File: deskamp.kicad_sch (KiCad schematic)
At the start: 33 parts, among them J1 Input 01, J2 Input 02, J3 Preamp Out, J4 Selector Switch, J5 LFE, J6 Mute, J7 Sleep, J8 Motor, J9 Power, K1 TQ2-12V, K2 TQ2-12V, K3 TQ2-12V, K4 TQ2-12V, Q1 PN2222A, Q2 PN2222A, Q3 PN2222A, Q4 PN2222A, U1 esp32-wemos-d1-mini, U2 L9110, U3 TSR_1-2433

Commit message: Change L9110 to Dip 8 footprint
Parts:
- U2: footprint L9110:so-8 -> Package_DIP:DIP-8_W7.62mm
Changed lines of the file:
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@@
 			)
 		)
-		(property "Footprint" "L9110:so-8"
+		(property "Footprint" "Package_DIP:DIP-8_W7.62mm"
 			(at 165.1 39.37 0)
 			(effects

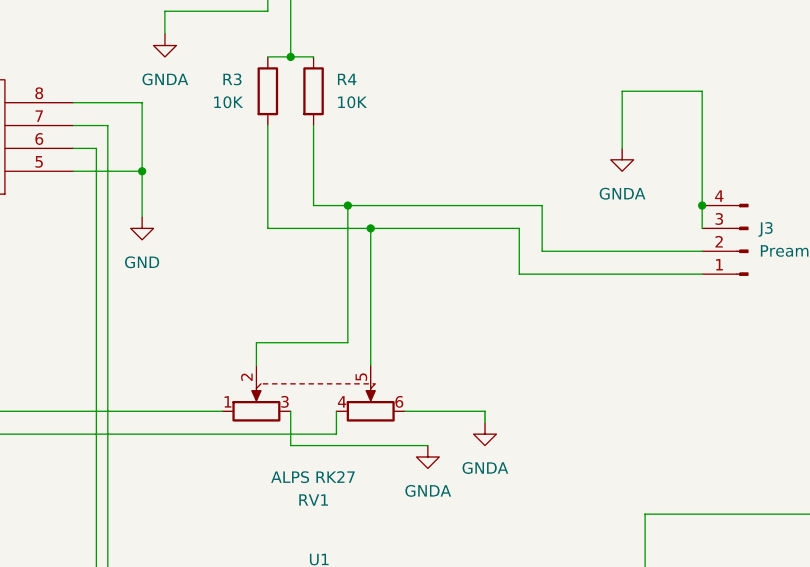
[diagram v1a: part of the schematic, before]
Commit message: Start routing signals
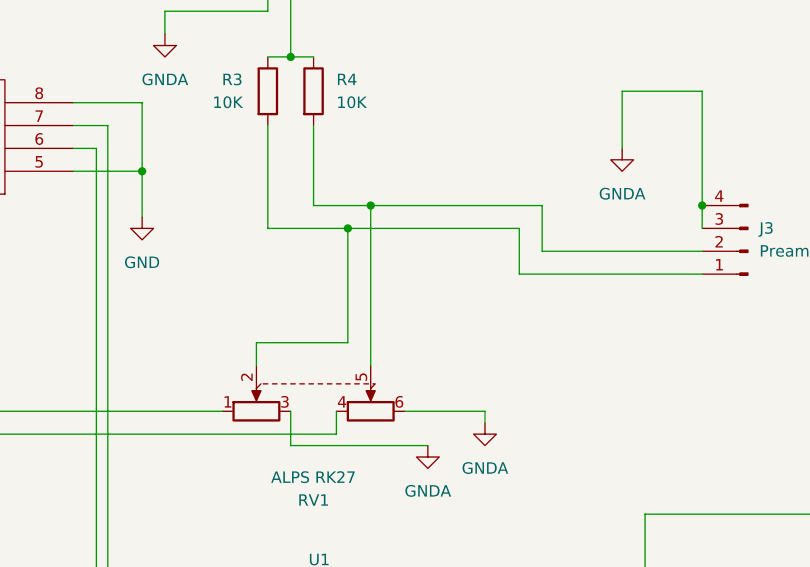
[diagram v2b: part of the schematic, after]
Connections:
- net at J3.1 (Pin_1), R3.2: now also RV1.2; no longer RV1.5
- net at J3.2 (Pin_2), R4.2: now also RV1.5; no longer RV1.2
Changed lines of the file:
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@@
 	)
 	(junction
-		(at 212.09 49.53)
+		(at 212.09 46.99)
 		(diameter 0)
 		(color 0 0 0 0)
@@
 	)
 	(junction
-		(at 209.55 46.99)
-		(diameter 0)
-		(color 0 0 0 0)
-	)
-	(junction
 		(at 151.13 38.1)
 		(diameter 0)
@@
 	)
 	(junction
+		(at 209.55 49.53)
+		(diameter 0)
+		(color 0 0 0 0)
+	)
+	(junction
 		(at 36.83 66.04)
 		(diameter 0)
@@
 	(wire
 		(pts
-			(xy 209.55 46.99) (xy 231.14 46.99)
+			(xy 205.74 46.99) (xy 212.09 46.99)
 		)
 		(stroke
@@
 	(wire
 		(pts
+			(xy 212.09 46.99) (xy 212.09 64.77)
+		)
+		(stroke
+			(width 0)
+			(type default)
+		)
+	)
+	(wire
+		(pts
 			(xy 92.71 96.52) (xy 92.71 113.03)
 		)
@@
 	(wire
 		(pts
+			(xy 212.09 46.99) (xy 231.14 46.99)
+		)
+		(stroke
+			(width 0)
+			(type default)
+		)
+	)
+	(wire
+		(pts
 			(xy 153.67 123.19) (xy 153.67 132.08)
 		)
@@
 	(wire
 		(pts
-			(xy 200.66 49.53) (xy 212.09 49.53)
+			(xy 200.66 49.53) (xy 209.55 49.53)
 		)
 		(stroke
@@
 	(wire
 		(pts
-			(xy 209.55 46.99) (xy 209.55 62.23)
-		)
-		(stroke
-			(width 0)
-			(type default)
-		)
-	)
-	(wire
-		(pts
 			(xy 166.37 55.88) (xy 166.37 115.57)
 		)
@@
 	(wire
 		(pts
+			(xy 209.55 49.53) (xy 209.55 62.23)
+		)
+		(stroke
+			(width 0)
+			(type default)
+		)
+	)
+	(wire
+		(pts
 			(xy 31.75 60.96) (xy 46.99 60.96)
 		)
@@
 	(wire
 		(pts
-			(xy 212.09 49.53) (xy 212.09 64.77)
-		)
-		(stroke
-			(width 0)
-			(type default)
-		)
-	)
-	(wire
-		(pts
 			(xy 129.54 140.97) (xy 193.04 140.97)
 		)
@@
 	(wire
 		(pts
-			(xy 212.09 49.53) (xy 228.6 49.53)
+			(xy 209.55 49.53) (xy 228.6 49.53)
 		)
 		(stroke
@@
 		)
 		(stroke
-			(width 0)
-			(type default)
-		)
-	)
-	(wire
-		(pts
-			(xy 205.74 46.99) (xy 209.55 46.99)
-		)
-		(stroke

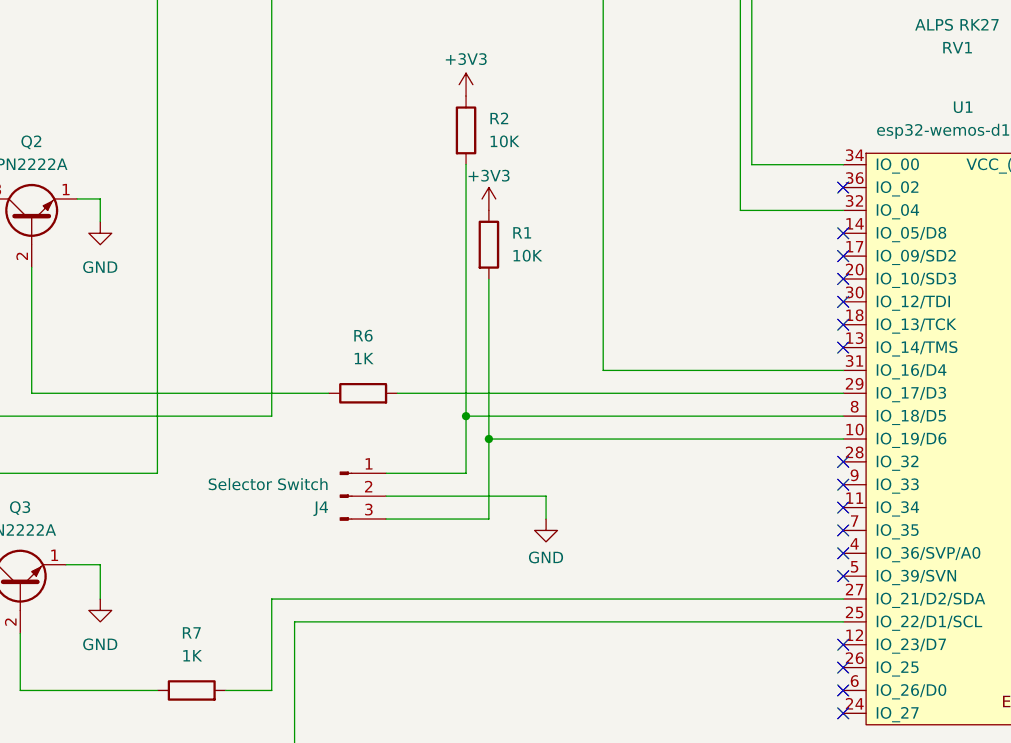
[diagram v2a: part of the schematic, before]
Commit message: Add mute selector pulldown
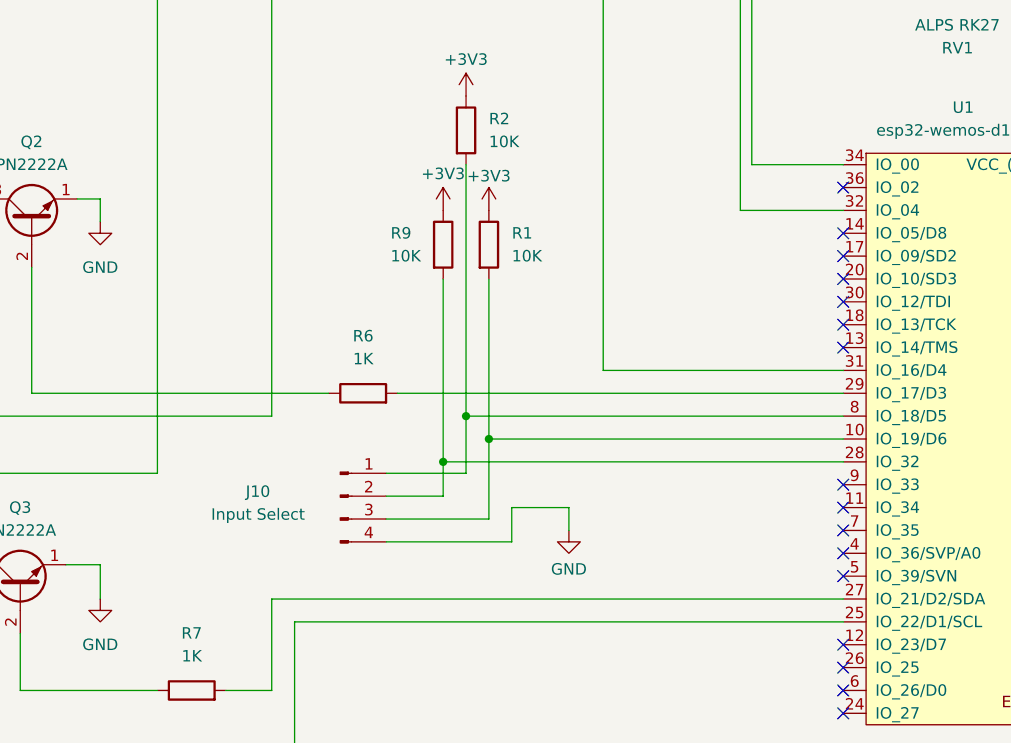
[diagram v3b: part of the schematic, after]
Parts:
- removed J4: Selector Switch, Connector_JST:JST_XH_B3B-XH-AM_1x03_P2.50mm_Vertical, symbol Connector:Conn_01x03_Pin
- added J10: Input Select, Connector_JST:JST_XH_B4B-XH-AM_1x04_P2.50mm_Vertical, symbol Connector:Conn_01x04_Pin
- added R9: 10K, Resistor_THT:R_Axial_DIN0204_L3.6mm_D1.6mm_P5.08mm_Horizontal, symbol Device:R
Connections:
- net +3V3: now also R9.1
- net GND: now also J10.4 (Pin_4)
- net at R2.2, U1.8 (IO_18/D5): now also J10.1 (Pin_1)
- net at R1.2, U1.10 (IO_19/D6): now also J10.3 (Pin_3)
- net at U1.28 (IO_32): now also J10.2 (Pin_2), R9.2
- no-connect marks 46 -> 45
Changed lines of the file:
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@@
 	)
 	(junction
+		(at 148.59 125.73)
+		(diameter 0)
+		(color 0 0 0 0)
+	)
+	(junction
 		(at 219.71 100.33)
 		(diameter 0)
@@
 	)
 	(no_connect
-		(at 193.04 125.73)
-	)
-	(no_connect
 		(at 193.04 153.67)
 	)
@@
 	(wire
 		(pts
+			(xy 156.21 134.62) (xy 156.21 130.81)
+		)
+		(stroke
+			(width 0)
+			(type default)
+		)
+	)
+	(wire
+		(pts
 			(xy 38.1 120.65) (xy 38.1 124.46)
 		)
@@
 	(wire
 		(pts
+			(xy 148.59 125.73) (xy 148.59 105.41)
+		)
+		(stroke
+			(width 0)
+			(type default)
+		)
+	)
+	(wire
+		(pts
 			(xy 193.04 92.71) (xy 182.88 92.71)
 		)
@@
 	(wire
 		(pts
+			(xy 142.24 129.54) (xy 148.59 129.54)
+		)
+		(stroke
+			(width 0)
+			(type default)
+		)
+	)
+	(wire
+		(pts
 			(xy 205.74 46.99) (xy 212.09 46.99)
 		)
@@
 	(wire
 		(pts
+			(xy 142.24 134.62) (xy 156.21 134.62)
+		)
+		(stroke
+			(width 0)
+			(type default)
+		)
+	)
+	(wire
+		(pts
 			(xy 153.67 123.19) (xy 153.67 132.08)
 		)
@@
 	(wire
 		(pts
-			(xy 160.02 129.54) (xy 142.24 129.54)
-		)
-		(stroke
-			(width 0)
-			(type default)
-		)
-	)
-	(wire
-		(pts
 			(xy 34.29 184.15) (xy 43.18 184.15)
 		)
@@
 	(wire
 		(pts
+			(xy 148.59 125.73) (xy 193.04 125.73)
+		)
+		(stroke
+			(width 0)
+			(type default)
+		)
+	)
+	(wire
+		(pts
 			(xy 55.88 186.69) (xy 62.23 186.69)
 		)
@@
 	(wire
 		(pts
+			(xy 148.59 129.54) (xy 148.59 125.73)
+		)
+		(stroke
+			(width 0)
+			(type default)
+		)
+	)
+	(wire
+		(pts
 			(xy 208.28 69.85) (xy 208.28 72.39)
 		)
@@
 	(wire
 		(pts
+			(xy 156.21 130.81) (xy 162.56 130.81)
+		)
+		(stroke
+			(width 0)
+			(type default)
+		)
+	)
+	(wire
+		(pts
 			(xy 48.26 118.11) (xy 62.23 118.11)
 		)
@@
 	(wire
 		(pts
-			(xy 160.02 132.08) (xy 160.02 129.54)
+			(xy 162.56 133.35) (xy 162.56 130.81)
 		)
 		(stroke
@@
 	)
 	(symbol
-		(lib_id "Connector:Conn_01x03_Pin")
-		(at 137.16 129.54 0)
-		(unit 1)
-		(exclude_from_sim no)
-		(in_bom yes)
-		(on_board yes)
-		(dnp no)
-		(property "Reference" "J4"
-			(at 135.89 130.8101 0)
-			(effects
-				(font
-					(size 1.27 1.27)
-				)
-				(justify right)
-			)
-		)
-		(property "Value" "Selector Switch"
-			(at 135.89 128.2701 0)
-			(effects
-				(font
-					(size 1.27 1.27)
-				)
-				(justify right)
-			)
-		)
-		(property "Footprint" "Connector_JST:JST_XH_B3B-XH-AM_1x03_P2.50mm_Vertical"
-			(at 137.16 129.54 0)
-			(effects
-				(font
-					(size 1.27 1.27)
-				)
-				(hide yes)
-			)
-		)
-		(property "Datasheet" "~"
-			(at 137.16 129.54 0)
-			(effects
-				(font
-					(size 1.27 1.27)
-				)
-				(hide yes)
-			)
-		)
-		(property "Description" "Generic connector, single row, 01x03, script generated"
-			(at 137.16 129.54 0)
-			(effects
-				(font
-					(size 1.27 1.27)
-				)
-				(hide yes)
-			)
-		)
-		(pin "2"
-		)
-		(pin "3"
-		)
-		(pin "1"
-		)
-		(instances
-			(project ""
-				(path "/59ddc706-9eaa-4fe8-a820-1bc51705c457"
-					(reference "J4")
-					(unit 1)
-				)
-			)
-		)
-	)
-	(symbol
 		(lib_id "Connector:Conn_01x04_Pin")
 		(at 26.67 60.96 0)
@@
 	)
 	(symbol
+		(lib_id "Connector:Conn_01x04_Pin")
+		(at 137.16 129.54 0)
+		(unit 1)
+		(exclude_from_sim no)
+		(in_bom yes)
+		(on_board yes)
+		(dnp no)
+		(property "Reference" "J10"
+			(at 128.016 129.032 0)
+			(effects
+				(font
+					(size 1.27 1.27)
+				)
+			)
+		)
+		(property "Value" "Input Select"
+			(at 128.016 131.572 0)
+			(effects
+				(font
+					(size 1.27 1.27)
+				)
+			)
+		)
+		(property "Footprint" "Connector_JST:JST_XH_B4B-XH-AM_1x04_P2.50mm_Vertical"
+			(at 137.16 129.54 0)
+			(effects
+				(font
+					(size 1.27 1.27)
+				)
+				(hide yes)
+			)
+		)
+		(property "Datasheet" "~"
+			(at 137.16 129.54 0)
+			(effects
+				(font
+					(size 1.27 1.27)
+				)
+				(hide yes)
+			)
+		)
+		(property "Description" "Generic connector, single row, 01x04, script generated"
+			(at 137.16 129.54 0)
+			(effects
+				(font
+					(size 1.27 1.27)
+				)
+				(hide yes)
+			)
+		)
+		(pin "1"
+		)
+		(pin "2"
+		)
+		(pin "3"
+		)
+		(pin "4"
+		)
+		(instances
+			(project ""
+				(path "/59ddc706-9eaa-4fe8-a820-1bc51705c457"
+					(reference "J10")
+					(unit 1)
+				)
+			)
+		)
+	)
+	(symbol
 		(lib_id "Device:R")
 		(at 200.66 34.29 0)
@@
 	(symbol
 		(lib_id "Device:R")
+		(at 148.59 101.6 0)
+		(unit 1)
+		(exclude_from_sim no)
+		(in_bom yes)
+		(on_board yes)
+		(dnp no)
+		(property "Reference" "R9"
+			(at 142.748 100.33 0)
+			(effects
+				(font
+					(size 1.27 1.27)
+				)
+				(justify left)
+			)
+		)
+		(property "Value" "10K"
+			(at 142.748 102.87 0)
+			(effects
+				(font
+					(size 1.27 1.27)
+				)
+				(justify left)
+			)
+		)
+		(property "Footprint" "Resistor_THT:R_Axial_DIN0204_L3.6mm_D1.6mm_P5.08mm_Horizontal"
+			(at 146.812 101.6 90)
+			(effects
+				(font
+					(size 1.27 1.27)
+				)
+				(hide yes)
+			)
+		)
+		(property "Datasheet" "~"
+			(at 148.59 101.6 0)
+			(effects
+				(font
+					(size 1.27 1.27)
+				)
+				(hide yes)
+			)
+		)
+		(property "Description" "Resistor"
+			(at 148.59 101.6 0)
+			(effects
+				(font
+					(size 1.27 1.27)
+				)
+				(hide yes)
+			)
+		)
+		(pin "1"
+		)
+		(pin "2"
+		)
+		(instances
+			(project "deskamp"
+				(path "/59ddc706-9eaa-4fe8-a820-1bc51705c457"
+					(reference "R9")
+					(unit 1)
+				)
+			)
+		)
+	)
+	(symbol
+		(lib_id "Device:R")
 		(at 134.62 55.88 90)
 		(unit 1)
@@
 	)
 	(symbol
+		(lib_id "power:+3V3")
+		(at 148.59 97.79 0)
+		(unit 1)
+		(exclude_from_sim no)
+		(in_bom yes)
+		(on_board yes)
+		(dnp no)
+		(property "Reference" "#PWR027"
+			(at 148.59 101.6 0)
+			(effects
+				(font
+					(size 1.27 1.27)
+				)
+				(hide yes)
+			)
+		)
+		(property "Value" "+3V3"
+			(at 148.59 93.726 0)
+			(effects
+				(font
+					(size 1.27 1.27)
+				)
+			)
+		)
+		(property "Footprint" ""
+			(at 148.59 97.79 0)
+			(effects
+				(font
+					(size 1.27 1.27)
+				)
+				(hide yes)
+			)
+		)
+		(property "Datasheet" ""
+			(at 148.59 97.79 0)
+			(effects
+				(font
+					(size 1.27 1.27)
+				)
+				(hide yes)
+			)
+		)
+		(property "Description" "Power symbol creates a global label with name \"+3V3\""
+			(at 148.59 97.79 0)
+			(effects
+				(font
+					(size 1.27 1.27)
+				)
+				(hide yes)
+			)
+		)
+		(pin "1"
+		)
+		(instances
+			(project "deskamp"
+				(path "/59ddc706-9eaa-4fe8-a820-1bc51705c457"
+					(reference "#PWR027")
+					(unit 1)
+				)
+			)
+		)
+	)
+	(symbol
 		(lib_id "power:GND")
-		(at 160.02 132.08 0)
+		(at 162.56 133.35 0)
 		(unit 1)
 		(exclude_from_sim no)
@@
 		(dnp no)
 		(property "Reference" "#PWR010"
-			(at 160.02 138.43 0)
+			(at 162.56 139.7 0)
 			(effects
 				(font
@@
 		)
 		(property "Value" "GND"
-			(at 160.02 136.398 0)
+			(at 162.56 137.668 0)
 			(effects
 				(font
@@
 		)
 		(property "Footprint" ""
-			(at 160.02 132.08 0)
+			(at 162.56 133.35 0)
 			(effects
 				(font
@@
 		)
 		(property "Datasheet" ""
-			(at 160.02 132.08 0)
+			(at 162.56 133.35 0)
 			(effects
 				(font
@@
 		)
 		(property "Description" "Power symbol creates a global label with name \"GND\" , ground"
-			(at 160.02 132.08 0)
+			(at 162.56 133.35 0)
 			(effects
 				(font

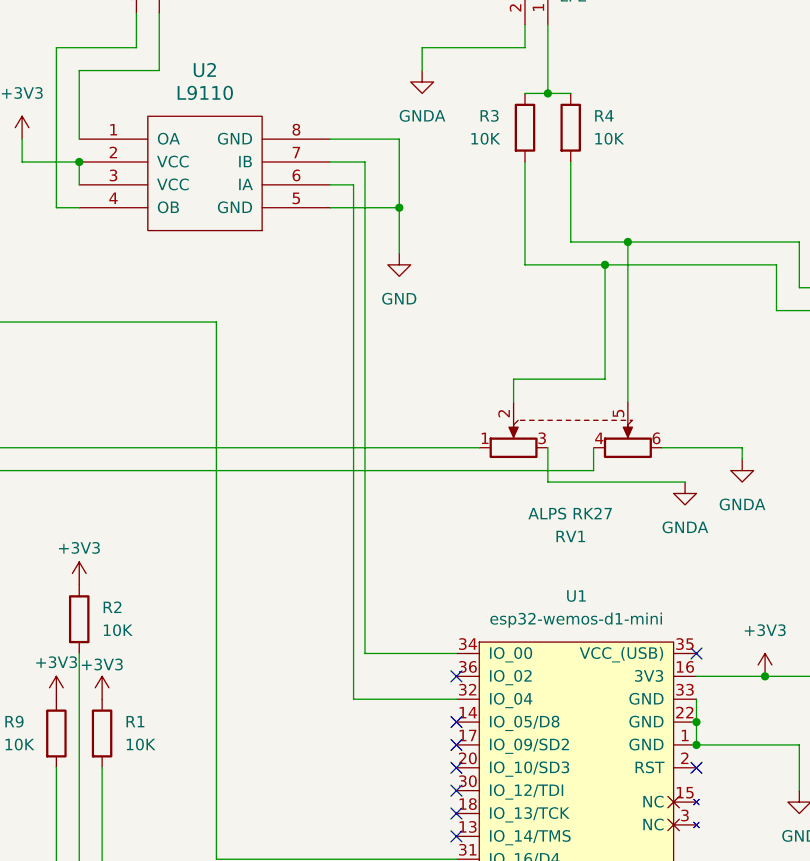
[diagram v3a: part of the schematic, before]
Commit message: Switch motor gpio for board layout
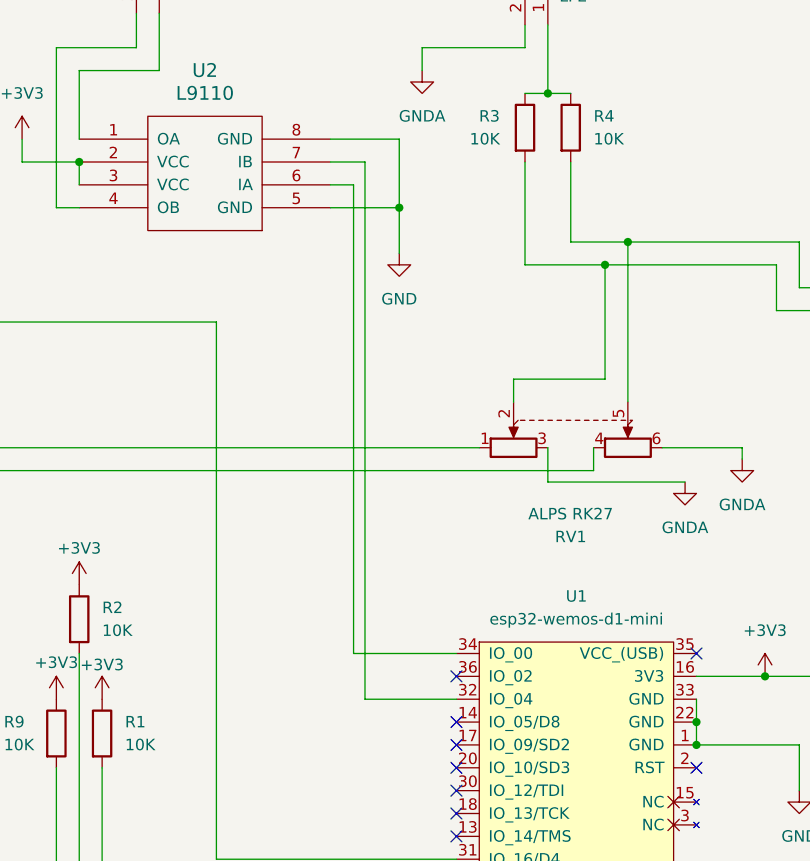
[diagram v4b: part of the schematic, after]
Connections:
- net at U2.6 (IA): now also U1.34 (IO_00); no longer U1.32 (IO_04)
- net at U2.7 (IB): now also U1.32 (IO_04); no longer U1.34 (IO_00)
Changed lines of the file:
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@@
-	(wire
-		(pts
-			(xy 193.04 92.71) (xy 182.88 92.71)
-		)
-		(stroke
-			(width 0)
-			(type default)
-		)
-	)
 	(wire
 		(pts
@@
 	(wire
 		(pts
-			(xy 181.61 40.64) (xy 181.61 97.79)
+			(xy 181.61 40.64) (xy 181.61 92.71)
 		)
 		(stroke
@@
 	(wire
 		(pts
+			(xy 193.04 97.79) (xy 182.88 97.79)
+		)
+		(stroke
+			(width 0)
+			(type default)
+		)
+	)
+	(wire
+		(pts
 			(xy 200.66 49.53) (xy 209.55 49.53)
 		)
@@
 	(wire
 		(pts
-			(xy 181.61 97.79) (xy 193.04 97.79)
-		)
-		(stroke
-			(width 0)
-			(type default)
-		)
-	)
-	(wire
-		(pts
 			(xy 101.6 177.8) (xy 101.6 181.61)
 		)
@@
 	(wire
 		(pts
-			(xy 182.88 38.1) (xy 182.88 92.71)
+			(xy 182.88 38.1) (xy 182.88 97.79)
 		)
 		(stroke
@@
 		)
 		(stroke
+			(width 0)
+			(type default)
+		)
+	)
+	(wire
+		(pts
+			(xy 181.61 92.71) (xy 193.04 92.71)
+		)
+		(stroke

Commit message: Ready for ground plane
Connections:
- net GND: now also J10.1 (Pin_1); no longer J10.4 (Pin_4)
- net at R8.2: now also U1.28 (IO_32); no longer U1.25 (IO_22/D1/SCL)
- net at U1.29 (IO_17/D3): now also J10.2 (Pin_2), R1.2; no longer R6.2
- net at U2.6 (IA): now also U1.32 (IO_04); no longer U1.34 (IO_00)
- net at U2.7 (IB): now also U1.34 (IO_00); no longer U1.32 (IO_04)
- net at U1.31 (IO_16/D4): now also J10.3 (Pin_3), R2.2; no longer R5.2
- net at U1.24 (IO_27): now also R5.2
- net at U1.26 (IO_25): now also R6.2
- net at U1.27 (IO_21/D2/SDA): no longer R7.2
- net at U1.30 (IO_12/TDI): now also R7.2
- new net: J10.4 (Pin_4), R9.2
- now unconnected: U1.10 (IO_19/D6), U1.8 (IO_18/D5)
- no-connect marks 45 -> 36

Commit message: Filled zones fun
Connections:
- net at J10.4 (Pin_4), R9.2: now also U1.37 (TD0)
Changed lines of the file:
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@@
 	(paper "A4")
 	(junction
+		(at 148.59 134.62)
+		(diameter 0)
+		(color 0 0 0 0)
+	)
+	(junction
 		(at 151.13 115.57)
 		(diameter 0)
@@
 		)
 		(stroke
+			(width 0)
+			(type default)
+		)
+	)
+	(wire
+		(pts
+			(xy 148.59 134.62) (xy 148.59 158.75)
+		)
+		(stroke
